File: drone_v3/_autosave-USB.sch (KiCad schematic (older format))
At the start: 4 parts, among them J1 USB_B_Micro, U2 USBLC6-2SC6

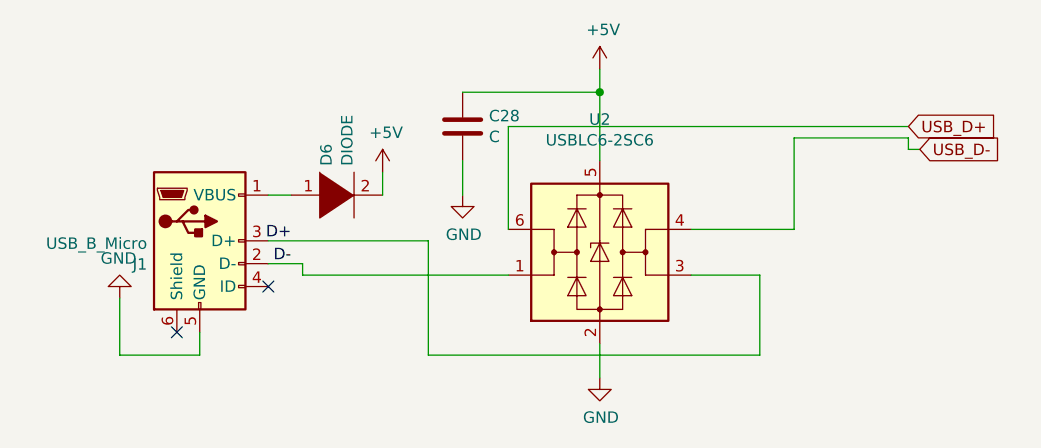
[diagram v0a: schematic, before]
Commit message: cystal layout
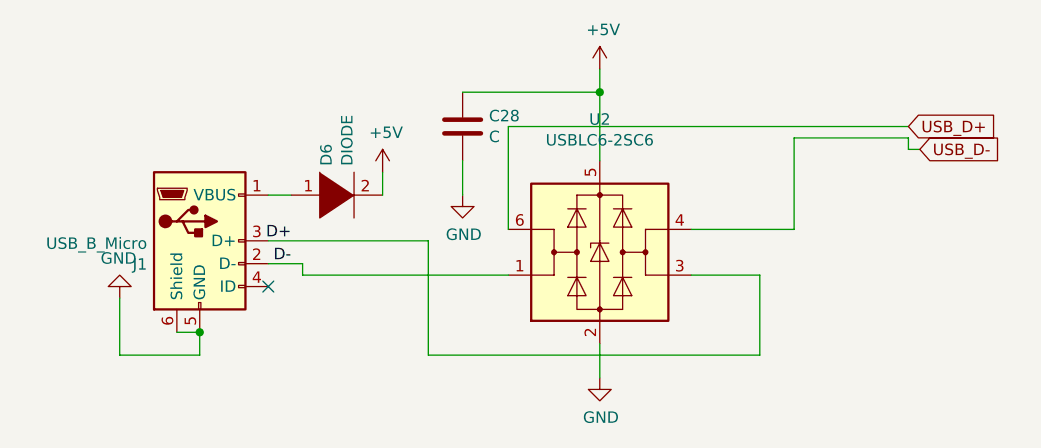
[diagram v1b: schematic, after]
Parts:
- D6: footprint Diode_SMD:D_0805_2012Metric_Pad1.15x1.40mm_HandSolder -> Diode_SMD:D_1206_3216Metric
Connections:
- net GND: now also J1.6 (Shield)
- no-connect marks 2 -> 1
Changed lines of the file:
@@
 	-1   0    0    1
 $EndComp
-NoConn ~ 3250 4000
 NoConn ~ 3650 3800
 Wire Wire Line
@@
 F 0 "D6" V 3904 3528 50  0000 L CNN
 F 1 "DIODE" V 3995 3528 50  0000 L CNN
-F 2 "Diode_SMD:D_0805_2012Metric_Pad1.15x1.40mm_HandSolder" H 3950 3400 50  0001 C CNN
+F 2 "Diode_SMD:D_1206_3216Metric" H 3950 3400 50  0001 C CNN
 F 3 "~" H 3950 3400 50  0001 C CNN
 	1    3950 3400
@@
 Wire Wire Line
 	4150 3400 4150 3300
+Wire Wire Line
+	3250 4000 3350 4000
+Connection ~ 3350 4000
 $EndSCHEMATC
